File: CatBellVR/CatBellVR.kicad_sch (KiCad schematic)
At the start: 1 part

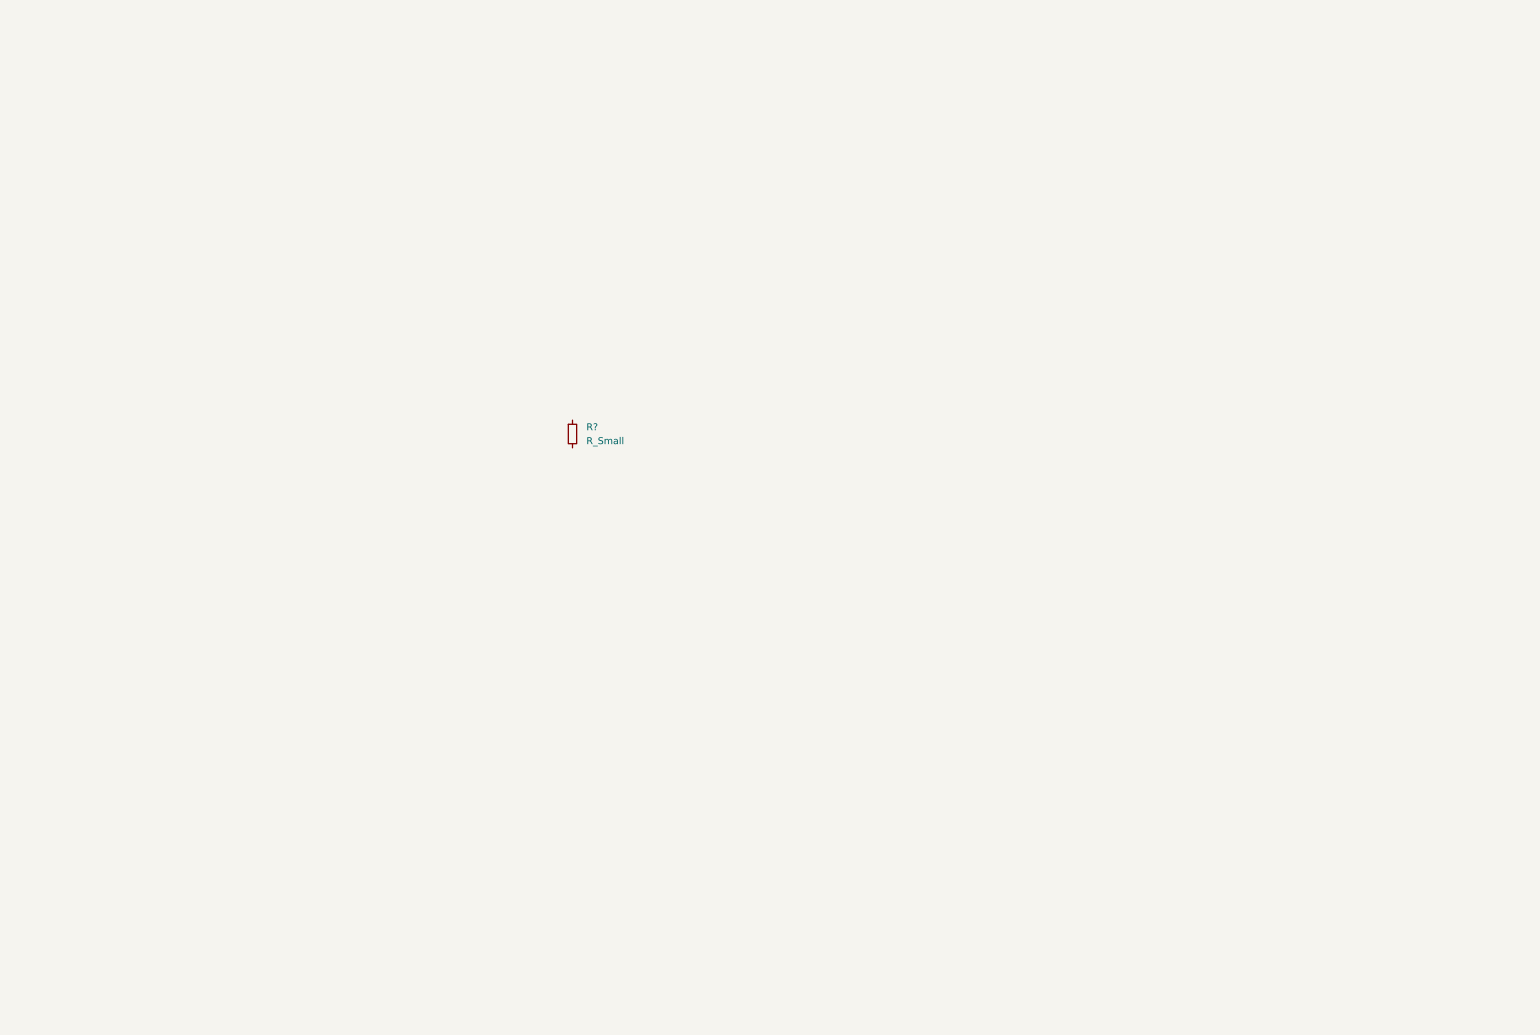
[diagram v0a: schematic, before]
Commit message: Added USB Type-C plug 2.0 port and sectioned off.
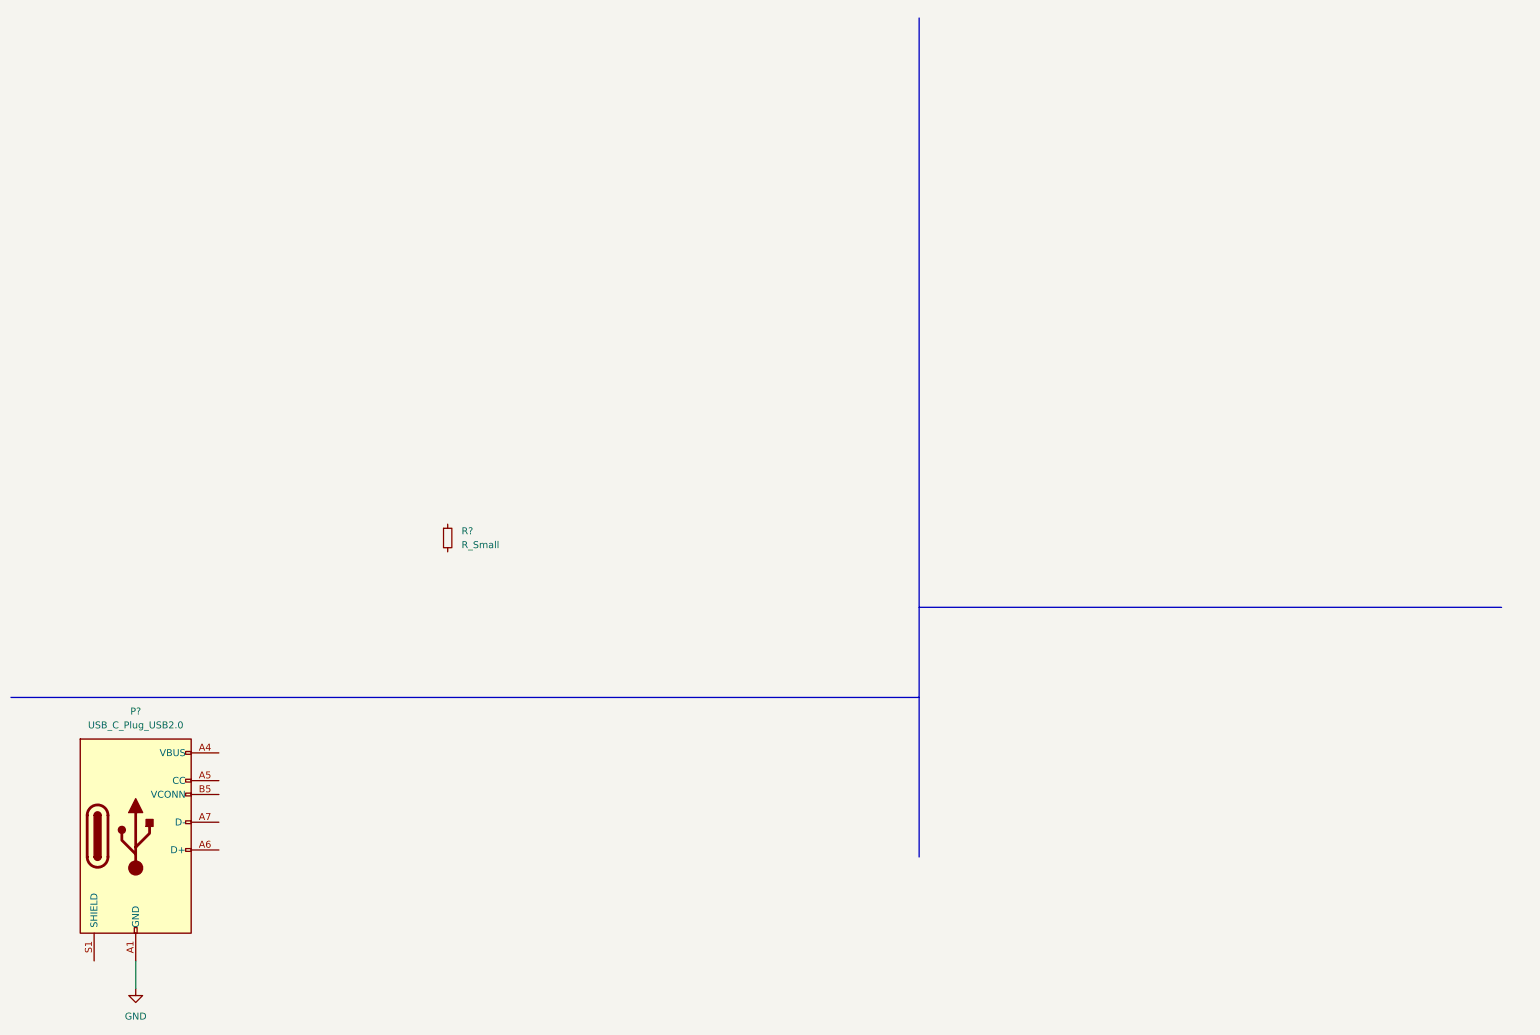
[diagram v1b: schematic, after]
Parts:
- added P?: USB_C_Plug_USB2.0, symbol Connector:USB_C_Plug_USB2.0
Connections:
- new net: P?.A4 (VBUS), P?.A9 (VBUS), P?.B4 (VBUS), P?.B9 (VBUS)
- new net GND: P?.A1 (GND), P?.A12 (GND), P?.B1 (GND), P?.B12 (GND)
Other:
- moved on the sheet: R?
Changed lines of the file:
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@@
 (kicad_sch (version 20211123) (generator eeschema)
   (paper "A4")
-  (symbol (lib_id "Device:R_Small") (at 114.3 88.9 0) (unit 1)
+  (polyline (pts (xy 177.8 120.65) (xy 284.48 120.65))
+    (stroke (width 0) (type default) (color 0 0 0 0))
+  )
+  (polyline (pts (xy 11.43 137.16) (xy 177.8 137.16))
+    (stroke (width 0) (type default) (color 0 0 0 0))
+  )
+  (wire (pts (xy 34.29 185.42) (xy 34.29 190.5))
+    (stroke (width 0) (type default) (color 0 0 0 0))
+  )
+  (polyline (pts (xy 177.8 12.7) (xy 177.8 166.37))
+    (stroke (width 0) (type default) (color 0 0 0 0))
+  )
+  (symbol (lib_id "power:GND") (at 34.29 190.5 0) (unit 1)
     (in_bom yes) (on_board yes) (fields_autoplaced)
-    (property "Reference" "R?" (id 0) (at 116.84 87.6299 0)
+    (property "Reference" "#PWR?" (id 0) (at 34.29 196.85 0)
+      (effects (font (size 1.27 1.27)) hide)
+    )
+    (property "Value" "GND" (id 1) (at 34.29 195.58 0))
+    (property "Footprint" "" (id 2) (at 34.29 190.5 0)
+      (effects (font (size 1.27 1.27)) hide)
+    )
+    (property "Datasheet" "" (id 3) (at 34.29 190.5 0)
+      (effects (font (size 1.27 1.27)) hide)
+    )
+    (pin "1")
+  )
+  (symbol (lib_id "Device:R_Small") (at 91.44 107.95 0) (unit 1)
+    (in_bom yes) (on_board yes) (fields_autoplaced)
+    (property "Reference" "R?" (id 0) (at 93.98 106.6799 0)
       (effects (font (size 1.27 1.27)) (justify left))
     )
-    (property "Value" "R_Small" (id 1) (at 116.84 90.1699 0)
+    (property "Value" "R_Small" (id 1) (at 93.98 109.2199 0)
       (effects (font (size 1.27 1.27)) (justify left))
     )
-    (property "Footprint" "" (id 2) (at 114.3 88.9 0)
+    (property "Footprint" "" (id 2) (at 91.44 107.95 0)
       (effects (font (size 1.27 1.27)) hide)
     )
-    (property "Datasheet" "~" (id 3) (at 114.3 88.9 0)
+    (property "Datasheet" "~" (id 3) (at 91.44 107.95 0)
       (effects (font (size 1.27 1.27)) hide)
     )
@@
     (pin "2")
   )
+  (symbol (lib_id "Connector:USB_C_Plug_USB2.0") (at 34.29 162.56 0) (unit 1)
+    (in_bom yes) (on_board yes) (fields_autoplaced)
+    (property "Reference" "P?" (id 0) (at 34.29 139.7 0))
+    (property "Value" "USB_C_Plug_USB2.0" (id 1) (at 34.29 142.24 0))
+    (property "Footprint" "" (id 2) (at 38.1 162.56 0)
+      (effects (font (size 1.27 1.27)) hide)
+    )
+    (property "Datasheet" "https://www.usb.org/sites/default/files/documents/usb_type-c.zip" (id 3) (at 38.1 162.56 0)
+      (effects (font (size 1.27 1.27)) hide)
+    )
+    (pin "A1")
+    (pin "A12")
+    (pin "A4")
+    (pin "A5")
+    (pin "A6")
+    (pin "A7")
+    (pin "A9")
+    (pin "B1")
+    (pin "B12")
+    (pin "B4")
+    (pin "B5")
+    (pin "B9")
+    (pin "S1")
+  )
   (sheet_instances
     (path "/" (page "1"))
   )
   (symbol_instances
+    (path "/34326806-2fa6-4d9e-a3f3-4beea1761d87"
+      (reference "#PWR?") (unit 1) (value "GND") (footprint "")
+    )
+    (path "/daf7c805-3c4a-4d53-bfa5-c5910798156f"
+      (reference "P?") (unit 1) (value "USB_C_Plug_USB2.0") (footprint "")
+    )
     (path "/525f23b9-a23c-4305-afe1-22811746f220"
       (reference "R?") (unit 1) (value "R_Small") (footprint "")

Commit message: Buttons are added, part of the battery center, the components of the usb section have just been added and the regulator section has been started.
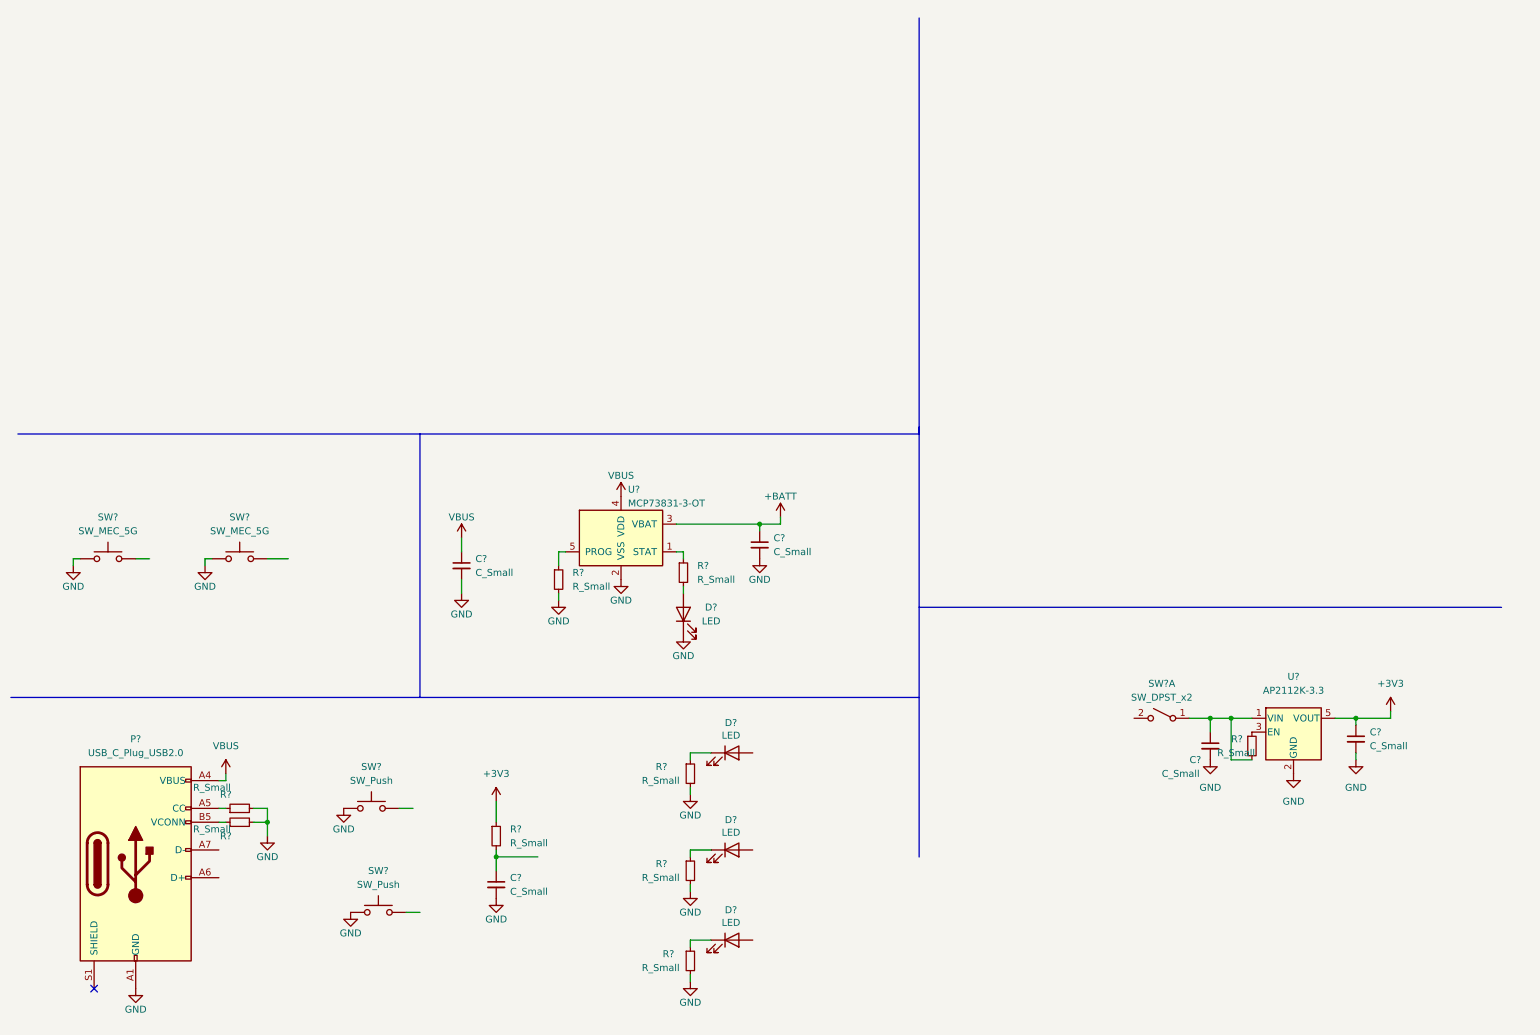
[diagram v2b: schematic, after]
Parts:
- removed R?: R_Small, symbol Device:R_Small
- added C? (x5): C_Small, symbol Device:C_Small
- added D? (x4): LED, LED_SMD:LED_0805_2012Metric, symbol Device:LED
- added R? (x9): R_Small, symbol Device:R_Small
- added SW? (x2): SW_MEC_5G, symbol Switch:SW_MEC_5G
- added SW? (x2): SW_Push, symbol Switch:SW_Push
- added SW?: SW_DPST_x2, symbol Switch:SW_DPST_x2
- added U?: AP2112K-3.3, Package_TO_SOT_SMD:SOT-23-5, symbol Regulator_Linear:AP2112K-3.3
- added U?: MCP73831-3-OT, Package_TO_SOT_SMD:SOT-23-5, symbol Battery_Management:MCP73831-3-OT
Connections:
- net GND: now also C?.2, C?.2, C?.2, C?.2, C?.2, D?.1 (K), R?.2, R?.2, R?.2, R?.2, R?.2, R?.2, SW?.1, SW?.1, SW?.1 (A), SW?.1 (A), SW?.2 (A), SW?.2 (A), U?.2 (GND), U?.2 (VSS)
- net VBUS: now reaches P?.A4 (VBUS), P?.A9 (VBUS), P?.B4 (VBUS), P?.B9 (VBUS)
- net VBUS: now also C?.1, U?.4 (VDD)
- net at P?.A5 (CC): now also R?.1
- net at P?.B5 (VCONN): now also R?.1
- new net: SW?.3 (B), SW?.4 (B) (x2)
- new net: C?.1, R?.2
- new net: C?.1, R?.2, SW?.1 (A), U?.1 (VIN)
- new net: R?.1, U?.3 (EN)
- new net: D?.1 (K), R?.1 (x3)
- new net: R?.1, U?.1 (STAT)
- new net: D?.2 (A), R?.2
- new net: R?.1, U?.5 (PROG)
- new net +3V3: C?.1, R?.1, U?.5 (VOUT)
- new net +BATT: C?.1, U?.3 (VBAT)
- no-connect marks 0 -> 1
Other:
- moved on the sheet: P?

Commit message: The entire schematic section was made, the ESP32-MINI was added as well as the conn_battery, as well as the corresponding labels, as a note, the ESP32-S2-MINI-1 library must be loaded
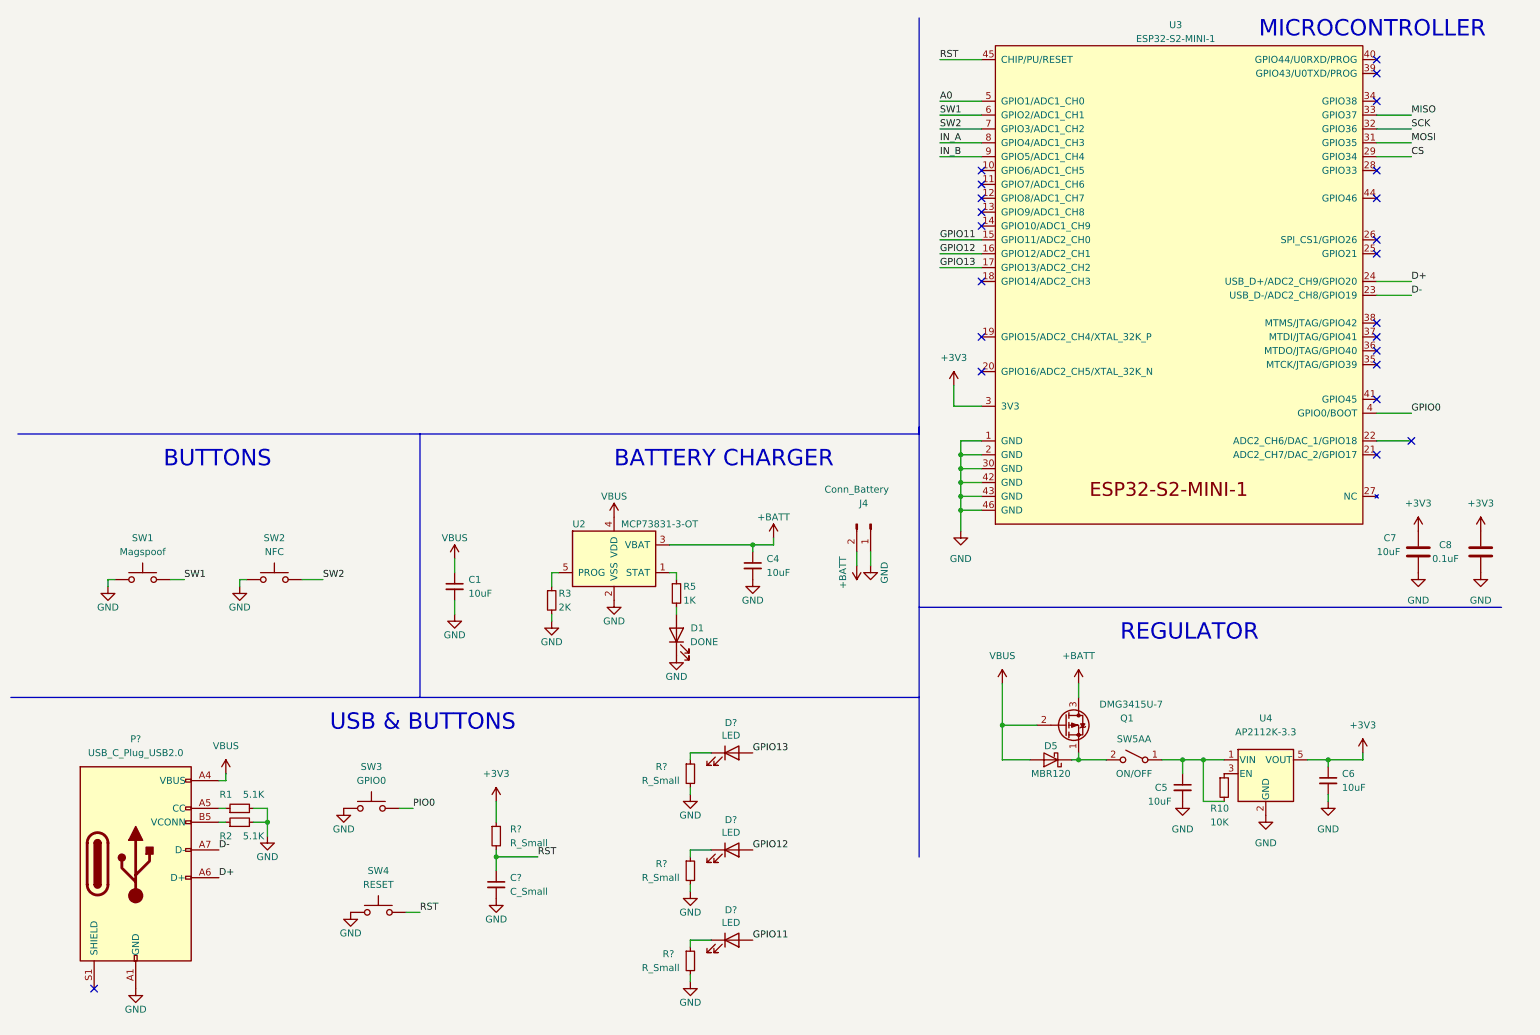
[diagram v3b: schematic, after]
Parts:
- added C7: 10uF, symbol Device:C
- added C8: 0.1uF, symbol Device:C
- added D5: MBR120, Diode_SMD:D_SOD-123F, symbol Diode:MBR1020VL
- added J4: Conn_Battery, symbol Connector:Conn_01x02_Male
- added Q1: DMG3415U-7, symbol Device:Q_PMOS_SGD
- added U3: ESP32-S2-MINI-1, Espressif:ESP32-S2-MINI-1, symbol Espressif:ESP32-S2-MINI-1
- C1, C4, C5, C6: renamed from C?; value C_Small -> 10uF
- D1: renamed from D?; value LED -> DONE
- R1, R2: renamed from R?; value R_Small -> 5.1K
- R10: renamed from R?; value R_Small -> 10K
- R3: renamed from R?; value R_Small -> 2K
- R5: renamed from R?; value R_Small -> 1K
- SW1: renamed from SW?; value SW_MEC_5G -> Magspoof
- SW2: renamed from SW?; value SW_MEC_5G -> NFC
- SW3: renamed from SW?; value SW_Push -> GPIO0
- SW4: renamed from SW?; value SW_Push -> RESET
- SW5A: renamed from SW?; value SW_DPST_x2 -> ON/OFF
- gave numbers to parts that had none: 2
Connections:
- net +3V3: now also C7.1, C8.1, U3.3 (3V3)
- net +BATT: now also J4.2 (Pin_2), Q1.3 (D)
- net GND: now also C7.2, C8.2, J4.1 (Pin_1), U3.1 (GND), U3.2 (GND), U3.30 (GND), U3.42 (GND), U3.43 (GND), U3.46 (GND)
- net VBUS: now also D5.2 (A), Q1.2 (G)
- net SW2: now reaches SW2.3 (B), SW2.4 (B)
- net SW2: now also U3.7 (GPIO3/ADC1_CH2)
- net RST: now reaches C?.1, R?.2
- net RST: now also SW4.2, U3.45 (CHIP/PU/RESET)
- net PIO0: now reaches SW3.2
- net SW1: now reaches SW1.3 (B), SW1.4 (B)
- net SW1: now also U3.6 (GPIO2/ADC1_CH1)
- net GPIO13: now reaches D?.2 (A)
- net GPIO13: now also U3.17 (GPIO13/ADC2_CH2)
- net GPIO12: now reaches D?.2 (A)
- net GPIO12: now also U3.16 (GPIO12/ADC2_CH1)
- net GPIO11: now reaches D?.2 (A)
- net GPIO11: now also U3.15 (GPIO11/ADC2_CH0)
- net D+: now reaches P?.A6 (D+)
- net D+: now also U3.24 (USB_D+/ADC2_CH9/GPIO20)
- net D-: now reaches P?.A7 (D-)
- net D-: now also U3.23 (USB_D-/ADC2_CH8/GPIO19)
- net at SW5A.2 (B): now also D5.1 (K), Q1.1 (S)
- new net A0: U3.5 (GPIO1/ADC1_CH0)
- new net CS: U3.29 (GPIO34)
- new net GPIO0: U3.4 (GPIO0/BOOT)
- new net IN_A: U3.8 (GPIO4/ADC1_CH3)
- new net IN_B: U3.9 (GPIO5/ADC1_CH4)
- new net MISO: U3.33 (GPIO37)
- new net MOSI: U3.31 (GPIO35)
- new net SCK: U3.32 (GPIO36)
- no-connect marks 1 -> 23
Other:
- note added: "BATTERY CHARGER"
- note added: "BUTTONS"
- note added: "MICROCONTROLLER"
- note added: "REGULATOR"
- note added: "USB & BUTTONS"
- moved on the sheet: C1, C4, C5, C6, D1, R10, R3, R5, SW1, SW2, SW5AA, U2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

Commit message: The I2C pins for the ESP32 have been located which are pins 17 and 18.
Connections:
- net GPIO13: no longer U3.17 (GPIO13/ADC2_CH2)
- net SCL: now reaches U3.18 (GPIO14/ADC2_CH3)
- new net SDA: U3.17 (GPIO13/ADC2_CH2)
- no-connect marks 23 -> 22
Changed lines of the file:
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@@
   (no_connect (at 261.62 22.86))
   (no_connect (at 261.62 27.94))
-  (no_connect (at 189.23 60.96))
   (no_connect (at 189.23 71.12))
   (no_connect (at 189.23 77.47))
@@
     (stroke (width 0) (type default) (color 0 0 0 0))
   )
+  (wire (pts (xy 181.61 60.96) (xy 189.23 60.96))
+    (stroke (width 0) (type default) (color 0 0 0 0))
+  )
   (wire (pts (xy 181.61 58.42) (xy 189.23 58.42))
     (stroke (width 0) (type default) (color 0 0 0 0))
@@
     (effects (font (size 1.27 1.27)) (justify left bottom))
   )
+  (label "SDA" (at 181.61 58.42 0)
+    (effects (font (size 1.27 1.27)) (justify left bottom))
+  )
   (label "MOSI" (at 267.97 35.56 0)
     (effects (font (size 1.27 1.27)) (justify left bottom))
@@
     (effects (font (size 1.27 1.27)) (justify left bottom))
   )
-  (label "GPIO13" (at 181.61 58.42 0)
-    (effects (font (size 1.27 1.27)) (justify left bottom))
-  )
   (label "SCK" (at 267.97 33.02 0)
     (effects (font (size 1.27 1.27)) (justify left bottom))
@@
     (effects (font (size 1.27 1.27)) (justify left bottom))
   )
+  (label "SCL" (at 181.61 60.96 0)
+    (effects (font (size 1.27 1.27)) (justify left bottom))
+  )
